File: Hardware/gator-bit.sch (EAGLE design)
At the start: 92 parts, among them J1 GATOR, J10 GATOR, J11 GATOR, J12 GATOR, J13 GATOR, J14 GATOR, J15 GATOR, J16 GATOR, J17 GATOR, J18 GATOR, J2 GATOR, J3 GATOR, J4 GATOR, J6 GATOR, J7 GATOR, J8 GATOR, J9 GATOR, U1 TPS63070, U2 micro:bit, U3 TXB0104, U4 ADJ REG 1.5A

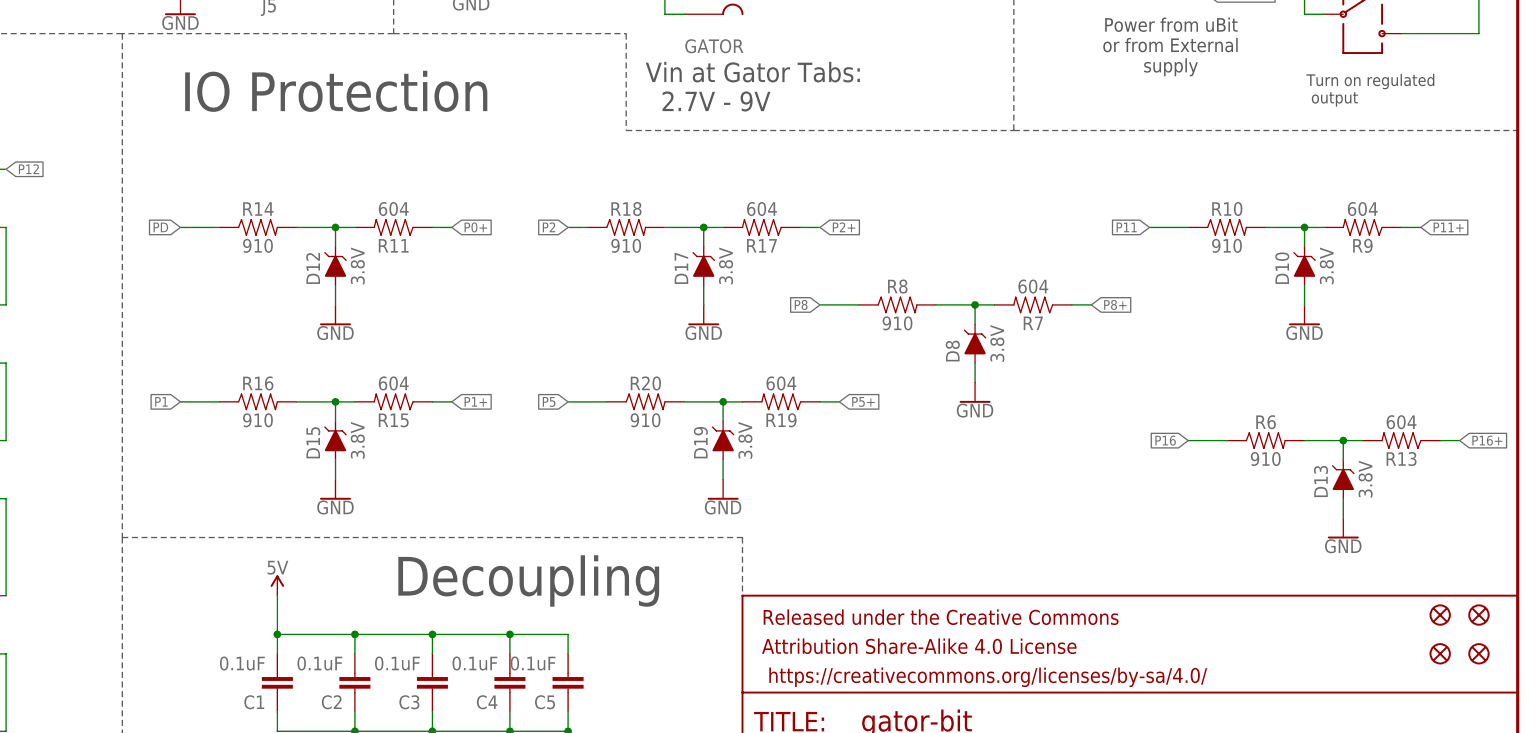
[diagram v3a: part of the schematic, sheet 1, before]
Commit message: added logos
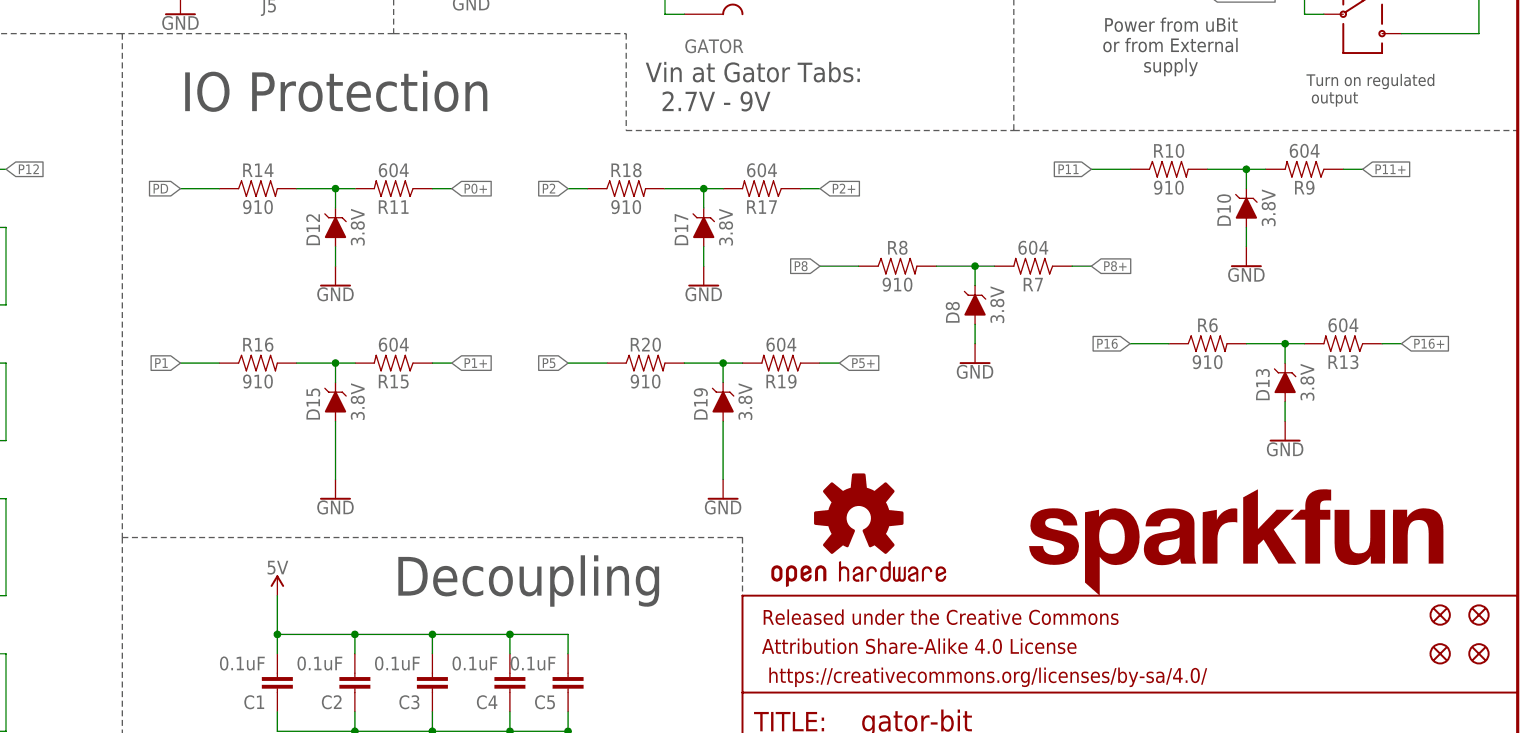
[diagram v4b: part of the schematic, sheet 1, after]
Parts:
- added LOGO1: OSHW-LOGOL, SparkFun-Aesthetics:OSHW-LOGOL
- added LOGO2: SFE_LOGO_NAME.1_INCH, SparkFun-Aesthetics:SFE_LOGO_NAME.1_INCH
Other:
- note added: "V02"
- note removed: "V01"
- moved on the sheet: D10, D12, D13, D15, D17, D19, D8, R10, R11, R13, R14, R15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

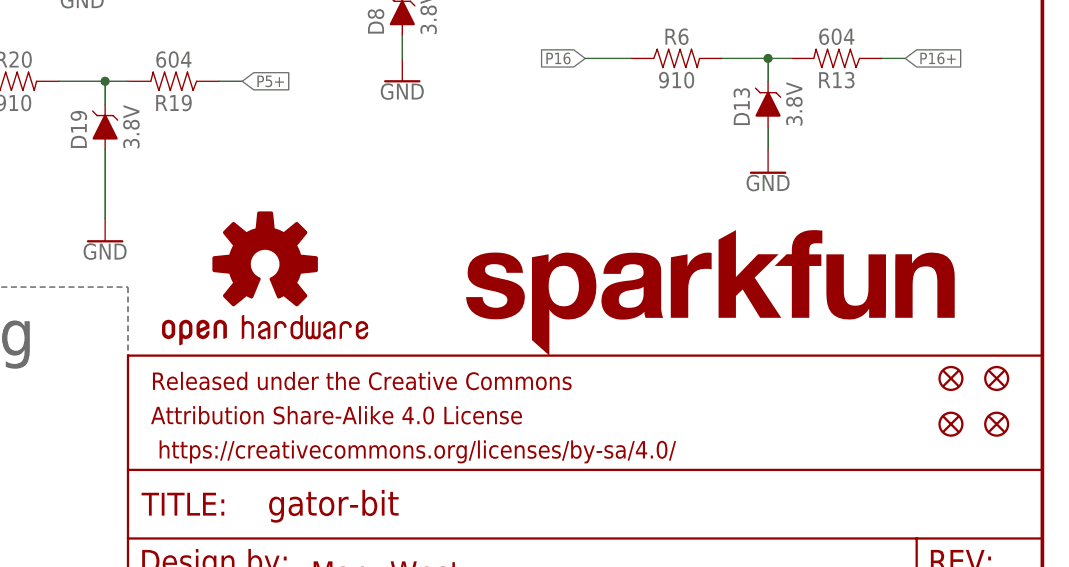
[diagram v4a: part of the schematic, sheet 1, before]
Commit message: Updating per QC Review
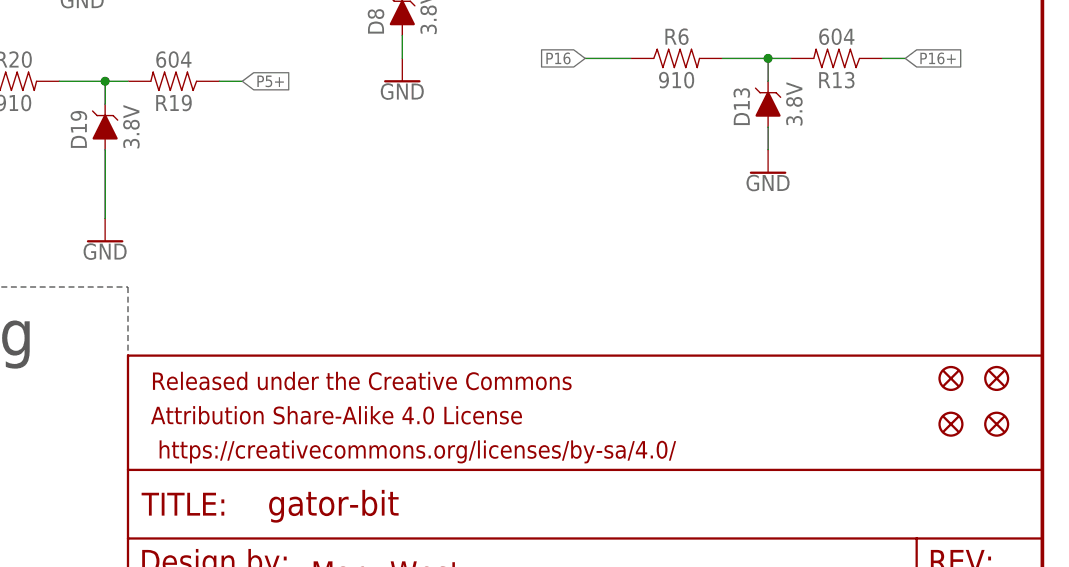
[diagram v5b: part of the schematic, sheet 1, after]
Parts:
- removed LOGO1: OSHW-LOGOL, SparkFun-Aesthetics:OSHW-LOGOL
- removed LOGO2: SFE_LOGO_NAME.1_INCH, SparkFun-Aesthetics:SFE_LOGO_NAME.1_INCH
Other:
- moved on the sheet: U3
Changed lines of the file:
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@@
 <?xml version="1.0" encoding="utf-8"?>
 <!DOCTYPE eagle SYSTEM "eagle.dtd">
-<eagle version="7.7.0">
+<eagle version="8.5.1">
 <drawing>
 <settings>
 <setting alwaysvectorfont="no"/>
+<setting keepoldvectorfont="yes"/>
 <setting verticaltext="up"/>
 </settings>
@@
 <part name="F1" library="SparkFun-Fuses" deviceset="PPTC" device="_HALF-AMP" value="6V/0.5A"/>
 <part name="SUPPLY3" library="SparkFun-PowerSymbols" deviceset="3.3V" device=""/>
-<part name="LOGO1" library="SparkFun-Aesthetics" deviceset="OSHW-LOGO" device="L"/>
-<part name="LOGO2" library="SparkFun-Aesthetics" deviceset="SFE_LOGO_NAME" device=".1_INCH"/>
 </parts>
 <sheets>
@@
 </instance>
 <instance part="SUPPLY3" gate="G$1" x="68.58" y="172.72"/>
-<instance part="LOGO1" gate="G$1" x="162.56" y="45.72"/>
-<instance part="LOGO2" gate="G$1" x="182.88" y="35.56"/>
 </instances>
 <busses>
@@
 <instance part="GND30" gate="1" x="215.9" y="96.52"/>
 <instance part="SUPPLY5" gate="G$1" x="241.3" y="119.38"/>
-<instance part="U3" gate="G$1" x="27.94" y="50.8"/>
-<instance part="SUPPLY7" gate="G$1" x="22.86" y="76.2"/>
-<instance part="SUPPLY8" gate="G$1" x="33.02" y="76.2"/>
-<instance part="GND31" gate="1" x="27.94" y="27.94"/>
+<instance part="U3" gate="G$1" x="45.72" y="50.8"/>
+<instance part="SUPPLY7" gate="G$1" x="40.64" y="76.2"/>
+<instance part="SUPPLY8" gate="G$1" x="50.8" y="76.2"/>
+<instance part="GND31" gate="1" x="45.72" y="27.94"/>
 <instance part="D7" gate="G$1" x="93.98" y="40.64"/>
 <instance part="D9" gate="G$1" x="106.68" y="40.64"/>
@@
 <segment>
 <pinref part="U3" gate="G$1" pin="GND"/>
-<wire x1="27.94" y1="35.56" x2="27.94" y2="30.48" width="0.1524" layer="91"/>
+<wire x1="45.72" y1="35.56" x2="45.72" y2="30.48" width="0.1524" layer="91"/>
 <pinref part="GND31" gate="1" pin="GND"/>
 </segment>
@@
 <wire x1="231.14" y1="142.24" x2="231.14" y2="149.86" width="0.1524" layer="91"/>
 <junction x="231.14" y="142.24"/>
+<junction x="210.82" y="142.24"/>
+<junction x="220.98" y="142.24"/>
 </segment>
 <segment>
 <pinref part="U3" gate="G$1" pin="VCCB"/>
-<wire x1="33.02" y1="68.58" x2="33.02" y2="76.2" width="0.1524" layer="91"/>
+<wire x1="50.8" y1="68.58" x2="50.8" y2="76.2" width="0.1524" layer="91"/>
 <pinref part="SUPPLY8" gate="G$1" pin="5V"/>
 </segment>
@@
 <pinref part="R12" gate="G$1" pin="2"/>
 <wire x1="48.26" y1="139.7" x2="48.26" y2="142.24" width="0.1524" layer="91"/>
+<junction x="48.26" y="142.24"/>
 </segment>
 <segment>
 <pinref part="U3" gate="G$1" pin="VCCA"/>
-<wire x1="22.86" y1="68.58" x2="22.86" y2="71.12" width="0.1524" layer="91"/>
+<wire x1="40.64" y1="68.58" x2="40.64" y2="71.12" width="0.1524" layer="91"/>
 <pinref part="SUPPLY7" gate="G$1" pin="3.3V"/>
 <pinref part="U3" gate="G$1" pin="OE"/>
-<wire x1="22.86" y1="71.12" x2="22.86" y2="76.2" width="0.1524" layer="91"/>
-<wire x1="12.7" y1="58.42" x2="5.08" y2="58.42" width="0.1524" layer="91"/>
-<wire x1="5.08" y1="58.42" x2="5.08" y2="71.12" width="0.1524" layer="91"/>
-<wire x1="5.08" y1="71.12" x2="22.86" y2="71.12" width="0.1524" layer="91"/>
-<junction x="22.86" y="71.12"/>
+<wire x1="40.64" y1="71.12" x2="40.64" y2="76.2" width="0.1524" layer="91"/>
+<wire x1="30.48" y1="58.42" x2="22.86" y2="58.42" width="0.1524" layer="91"/>
+<wire x1="22.86" y1="58.42" x2="22.86" y2="71.12" width="0.1524" layer="91"/>
+<wire x1="22.86" y1="71.12" x2="40.64" y2="71.12" width="0.1524" layer="91"/>
+<junction x="40.64" y="71.12"/>
 </segment>
 </net>
@@
 <segment>
 <pinref part="U3" gate="G$1" pin="A1"/>
-<wire x1="12.7" y1="53.34" x2="10.16" y2="53.34" width="0.1524" layer="91"/>
-<label x="10.16" y="53.34" size="1.27" layer="95" rot="R180" xref="yes"/>
+<wire x1="30.48" y1="53.34" x2="27.94" y2="53.34" width="0.1524" layer="91"/>
+<label x="27.94" y="53.34" size="1.27" layer="95" rot="R180" xref="yes"/>
 </segment>
 </net>
@@
 <segment>
 <pinref part="U3" gate="G$1" pin="B1"/>
-<wire x1="43.18" y1="53.34" x2="45.72" y2="53.34" width="0.1524" layer="91"/>
-<label x="45.72" y="53.34" size="1.27" layer="95" xref="yes"/>
-</segment>
-</net>
+<wire x1="60.96" y1="53.34" x2="63.5" y2="53.34" width="0.1524" layer="91"/>
+<label x="63.5" y="53.34" size="1.27" layer="95" xref="yes"/>
+</segment>
+</net>
